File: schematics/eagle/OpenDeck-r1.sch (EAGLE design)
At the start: 249 parts, among them U1 ATMEGA32U4-AU, U2 4067D, U3 4067D, U4 74AC11238D, U5 ULN2803, U6 74AC165D, U7 74AC11238D, U8 6N138, Y1 16MHz

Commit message: LDO for analog, charge pump for LEDs, misc
* added LDO for AREF and to power analog circuitry
* added charge pump to provide stable 5V for LEDs
* remove one row in LED matrix so that 48 LEDs = 16 RGB LEDs
* move SR_LATCH to PD0
* better capacitor markings
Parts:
- removed L49, L50, L51, L52, L53, L54, L55, L56: LAW51M, led:LAW51M
- removed LM4132CMF-4.1: LM4132BMF-4.1, NSC_By_element14_Batch_1.1:LM4132BMF-4.1
- removed R7: 75, rcl:R-EU_0204/7
- added C18: 1u, rcl:C-EU025-025X050
- added C19: 0.47u, rcl:C-EU025-025X050
- added C20, C21, C22: 0.1u, rcl:C-EU025-025X050
- added MAX1595-5V: MAX662CPA, maxim:MAX662CPA
- added MCP1825-3.3V: MCP1825_SOT223, bt_regulator:MCP1825_SOT223
- added Q1, Q2, Q3, Q4, Q5, Q6: FDN360P, transistor-power:FDN360P
- C1, C10, C11, C12, C13, C14, C17, C6, C7, C8, C9: value 0.01 -> 0.01u
- C2: value 0.01 -> 4.7u
- C3: value 0.01 -> 1u
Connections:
- removed net LR_7: R7.2, U1.PD0(INT0/OC0B/SCL)
- removed net L_ROW_6: L49G$1.A, L50G$1.A, L51G$1.A, L52G$1.A, L53G$1.A, L54G$1.A, L55G$1.A, L56G$1.A, R7.1
- removed net SR_CLOCK/MISO: HEADER_1.4, U1.PB3(PDO/MISO), U6A.CLK
- new net +5V_LEDS: C19.1, MAX1595-5V.AOUT, MAX1595-5V.VOUT, Q1.S, Q2.S, Q3.S, Q4.S, Q5.S, Q6.S
- new net MISO: HEADER_1.4, U1.PB3(PDO/MISO)
- new net N$74: C20.1, MAX1595-5V.CXP
- new net N$78: C20.2, MAX1595-5V.CXN
- new net N$79: Q1.D, R1.2
- new net N$80: Q2.D, R2.2
- new net N$81: Q3.D, R3.2
- new net N$82: Q4.D, R4.2
- new net N$83: Q5.D, R5.2
- new net N$86: Q6.D, R6.2
- new net SR_CLOCK: U1.PD1(INT1/SDA), U6A.CLK
- net +5V: now also C18.1, MAX1595-5V.SHDN, MAX1595-5V.VCC, MCP1825-3.3V.VIN; no longer LM4132CMF-4.1.EN, LM4132CMF-4.1.VIN, U2P.VDD, U3P.VDD
- net AREF: now also C21.2, C22.2, MCP1825-3.3V.VOUT, U2P.VDD, U3P.VDD; no longer LM4132CMF-4.1.VREF
- net GND: now also C18.2, C19.2, C21.1, C22.1, MAX1595-5V.GND, MAX1595-5V.PGND, MCP1825-3.3V.GND, MCP1825-3.3V.HEATSINK; no longer LM4132CMF-4.1.GND
- net LC_1: no longer L49G$1.C
- net LC_2: no longer L50G$1.C
- net LC_3: no longer L51G$1.C
- net LC_4: no longer L52G$1.C
- net LC_5: no longer L53G$1.C
- net LC_6: no longer L54G$1.C
- net LC_7: no longer L55G$1.C
- net LC_8: no longer L56G$1.C
- net LR_1: now also Q1.G; no longer R1.2
- net LR_2: now also Q2.G; no longer R2.2
- net LR_3: now also Q3.G; no longer R3.2
- net LR_4: now also Q4.G; no longer R4.2
- net LR_5: now also Q5.G; no longer R5.2
- net LR_6: now also Q6.G; no longer R6.2
- net SR_LATCH: now also U1.PD0(INT0/OC0B/SCL); no longer U1.PD1(INT1/SDA)
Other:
- note added: "LEDs"
- note added: "Note: All diodes 1N4148 Transistors: FDC6312P"
- note removed: "Note: All diodes 1N4148"
- moved on the sheet: C11, C2, C3, C7, C9, L01, L02, L03, L04, L05, L06, L07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

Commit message: * added protection diodes for VBUS, D- and D+ * board can be powered with USB connector only to reduce complexity - either via PC or mobile charger/similar
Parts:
- removed 22: 22, rcl:R-EU_0204/7
- removed C15, C16: 10u, rcl:CPOL-EUSMCB
- removed C6: 0.01u, rcl:C-EU025-025X050
- removed JP2: POWER_JACKPTH, SparkFun-Connectors:POWER_JACKPTH
- removed NCP1117ST50T3G: MC33269ST-3.3T3, linear:MC33269ST-3.3T3
- added C23: 10u, rcl:CPOL-EUSMCB
- added C24: 1u, rcl:C-EU025-025X050
- added PRTR5V0U2X: PRTR5V0U2X, PRTR5V0U2X:PRTR5V0U2X
- added R7: 22, rcl:R-EU_0204/7
- C10, C11, C12, C13, C14, C17, C7, C8, C9: value 0.01u -> 0.1u
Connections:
- removed net N$6: JP1.D+, R22.1
- removed net N$73: 22.1, JP1.D-
- removed net VIN: C16.+, JP2.PWR, NCP1117ST50T3G.IN
- new net D+X: JP1.D+, PRTR5V0U2X.I/O2, R22.1
- new net D-X: JP1.D-, PRTR5V0U2X.I/O1, R7.1
- net +5V: now also C23.+, C24.1, PRTR5V0U2X.VCC; no longer C15.+, C6.1, NCP1117ST50T3G.OUT, NCP1117ST50T3G.OUT@1
- net D-: now also R7.2; no longer 22.2
- net GND: now also C23.-, C24.2, PRTR5V0U2X.GND; no longer C15.-, C16.-, C6.2, JP2.GND, JP2.GNDBREAK, NCP1117ST50T3G.GND/ADJ
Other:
- note added: "Notes: All diodes 1N4148 Transistors: FDC6312P TVS diodes: PRTR5V0U2X"
- note removed: "Note: All diodes 1N4148 Transistors: FDC6312P"
- note removed: "POWER JACK"
- note removed: "VBUS"
- moved on the sheet: JP1, POWER_LED, R22, R23

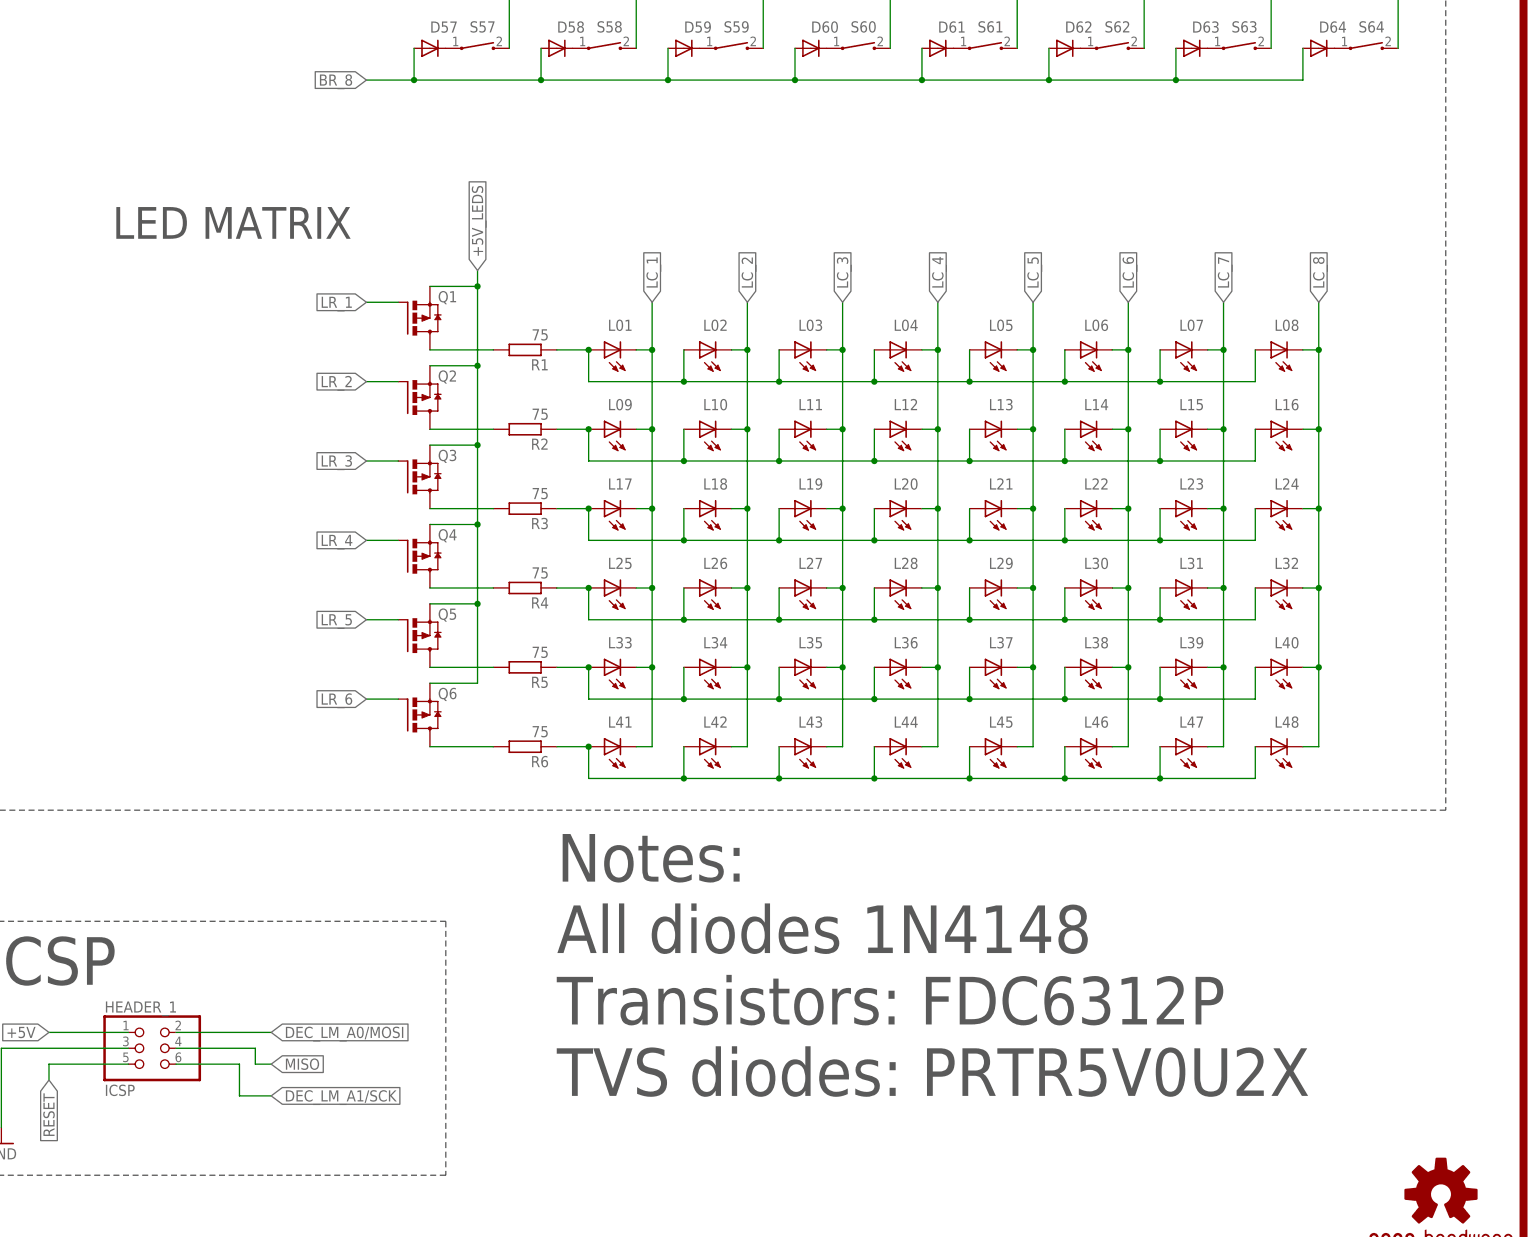
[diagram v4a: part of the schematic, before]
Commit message: changes to led matrix
* replace 75R with 100R resistors for LED rows
* add 4k7 pull-up on each row transistor
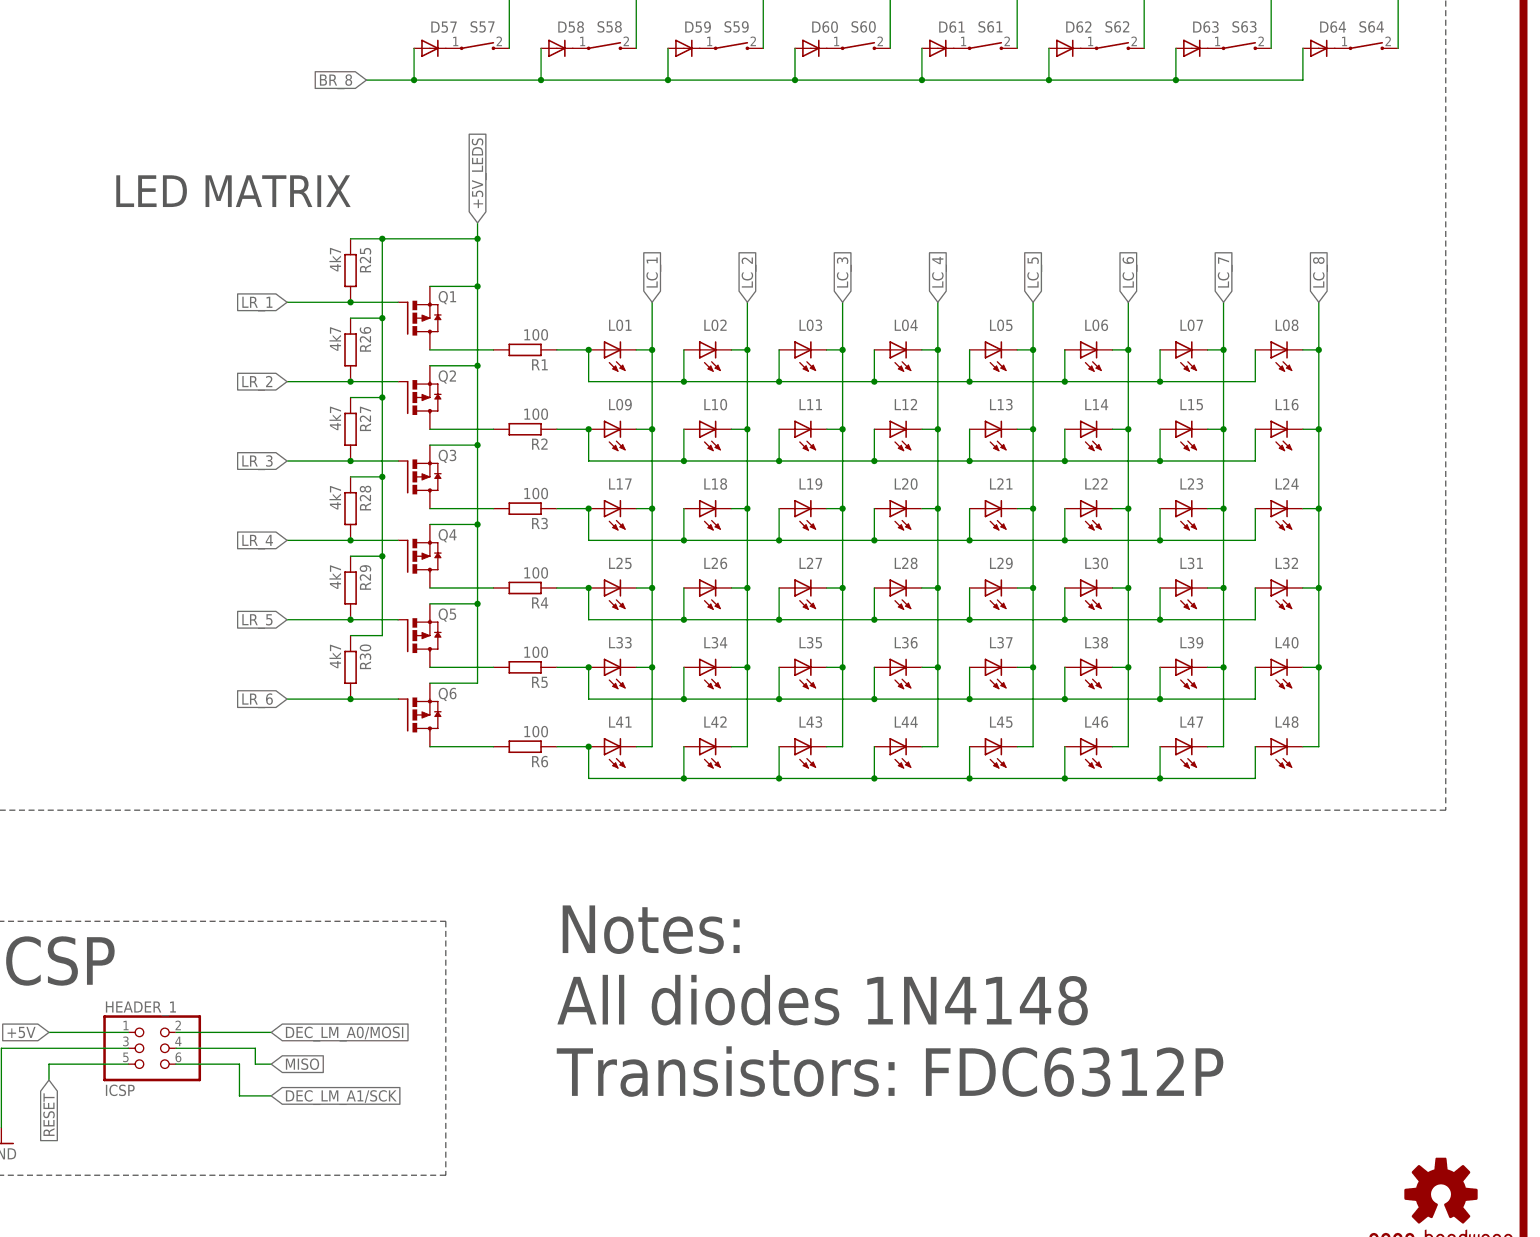
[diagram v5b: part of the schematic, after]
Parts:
- added R25, R26, R27, R28, R29, R30: 4k7, rcl:R-EU_0204/7
- R1, R2, R3, R4, R5, R6: value 75 -> 100
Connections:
- net +5V_LEDS: now also R25.1, R26.1, R27.1, R28.1, R29.1, R30.1
- net LR_1: now also R25.2
- net LR_2: now also R26.2
- net LR_3: now also R27.2
- net LR_4: now also R28.2
- net LR_5: now also R29.2
- net LR_6: now also R30.2
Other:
- note added: "Notes: All diodes 1N4148 Transistors: FDC6312P"
- note removed: "Notes: All diodes 1N4148 Transistors: FDC6312P TVS diodes: PRTR5V0U2X"

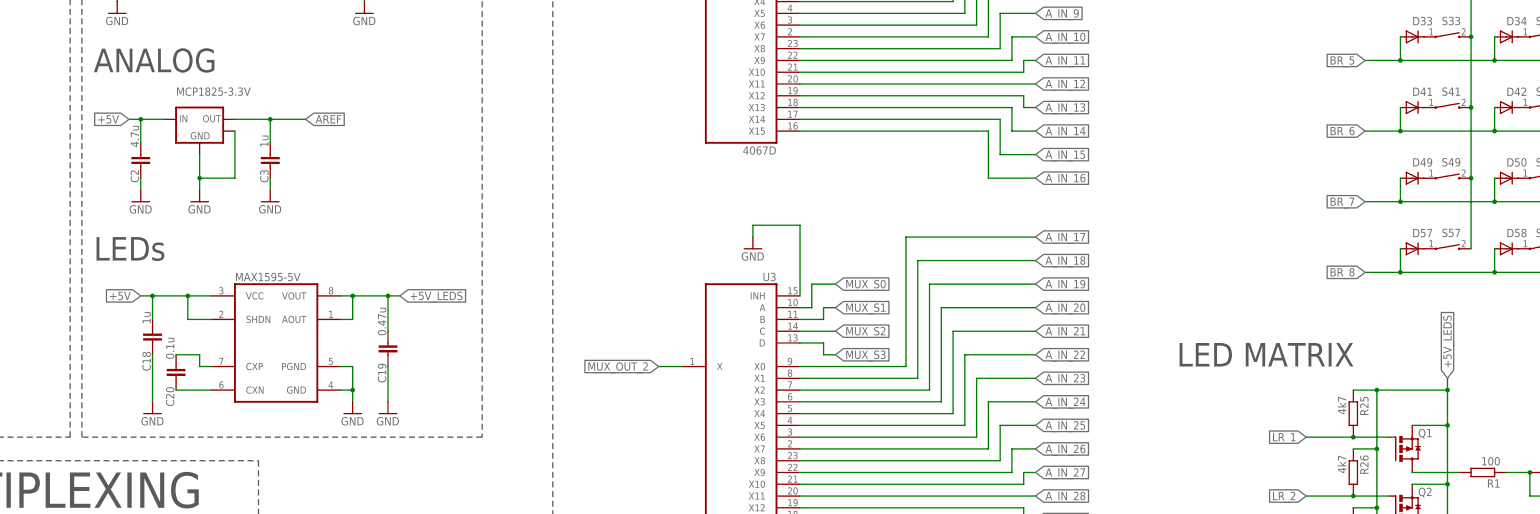
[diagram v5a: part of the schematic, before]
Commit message: replace charge pump for LEDs with LDO (cost)
* max1595 5V charge pump is replaced with LP2985 4V LDO for cost reasons
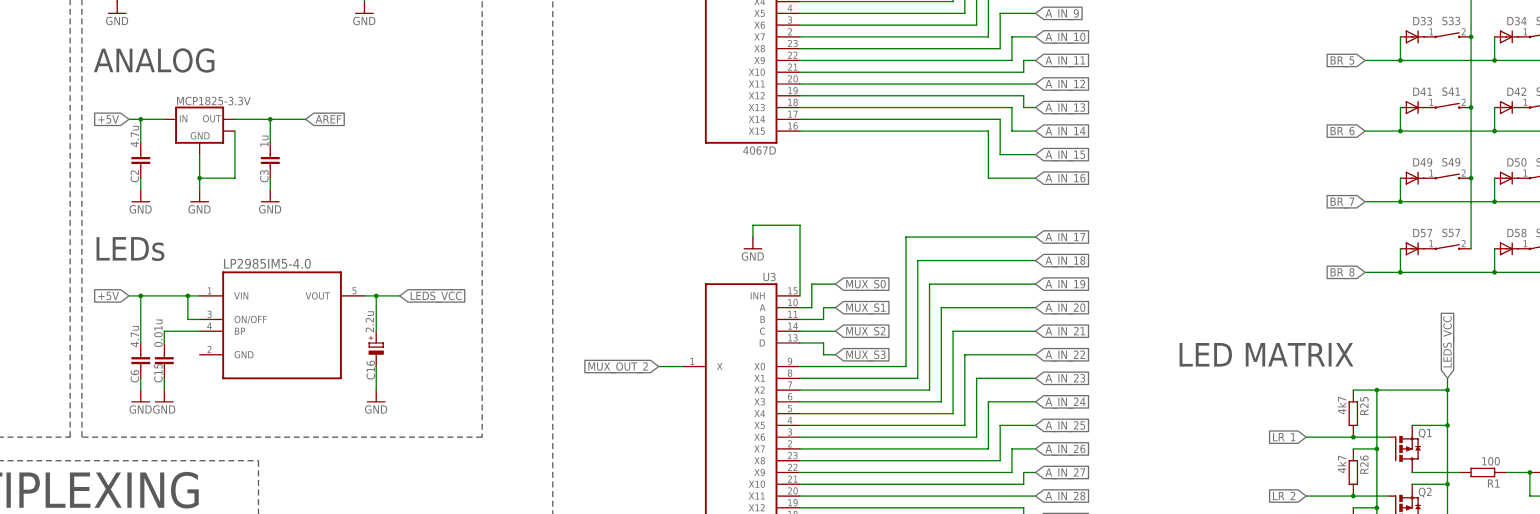
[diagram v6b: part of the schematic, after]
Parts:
- removed C18: 1u, rcl:C-EU025-025X050
- removed C19: 0.47u, rcl:C-EU025-025X050
- removed C20: 0.1u, rcl:C-EU025-025X050
- removed MAX1595-5V: MAX662CPA, maxim:MAX662CPA
- added C15: 0.01u, rcl:C-EU025-025X050
- added C16: 2.2u, rcl:CPOL-EUSMCB
- added C6: 4.7u, rcl:C-EU025-025X050
- added U9: LP2985IM5-4.0, NSC_By_element14_Batch_1.1:LP2985IM5-4.0
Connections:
- removed net +5V_LEDS: C19.1, MAX1595-5V.AOUT, MAX1595-5V.VOUT, Q1.S, Q2.S, Q3.S, Q4.S, Q5.S, Q6.S, R25.1, R26.1, R27.1, R28.1, R29.1, R30.1
- removed net N$74: C20.1, MAX1595-5V.CXP
- removed net N$78: C20.2, MAX1595-5V.CXN
- new net LEDS_VCC: C16.+, Q1.S, Q2.S, Q3.S, Q4.S, Q5.S, Q6.S, R25.1, R26.1, R27.1, R28.1, R29.1, R30.1, U9.VOUT
- new net N$6: C15.1, U9.BP
- net +5V: now also C6.1, U9.ON/OFF, U9.VIN; no longer C18.1, MAX1595-5V.SHDN, MAX1595-5V.VCC
- net GND: now also C15.2, C16.-, C6.2; no longer C18.2, C19.2, MAX1595-5V.GND, MAX1595-5V.PGND

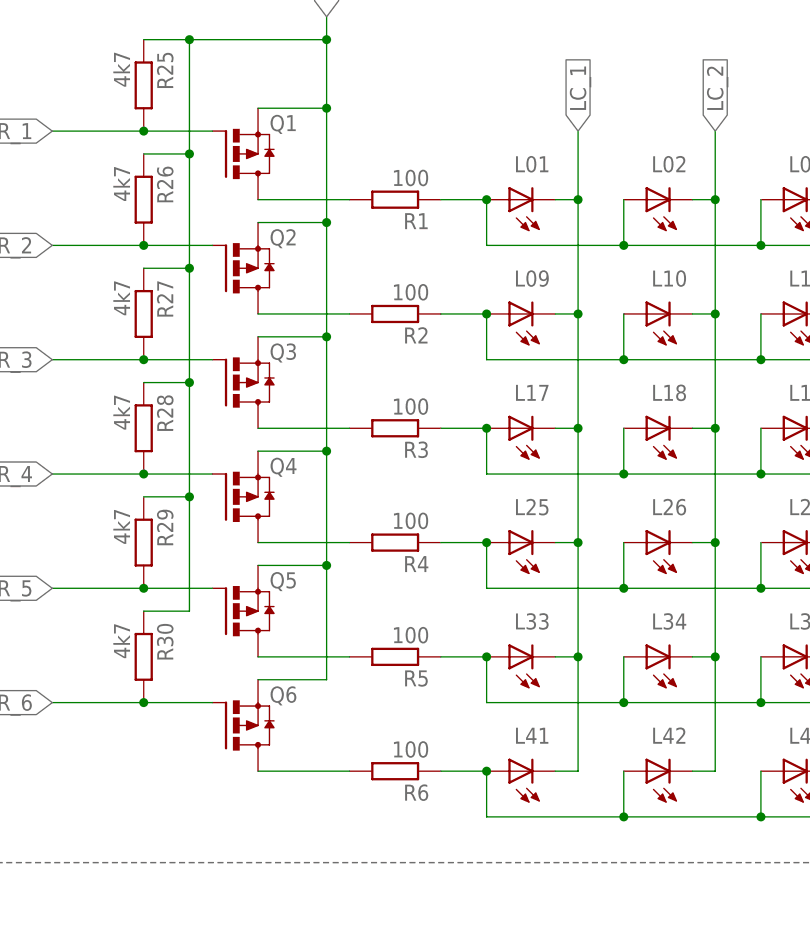
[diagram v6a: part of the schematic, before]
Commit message: replace 100R with 75R for LEDs
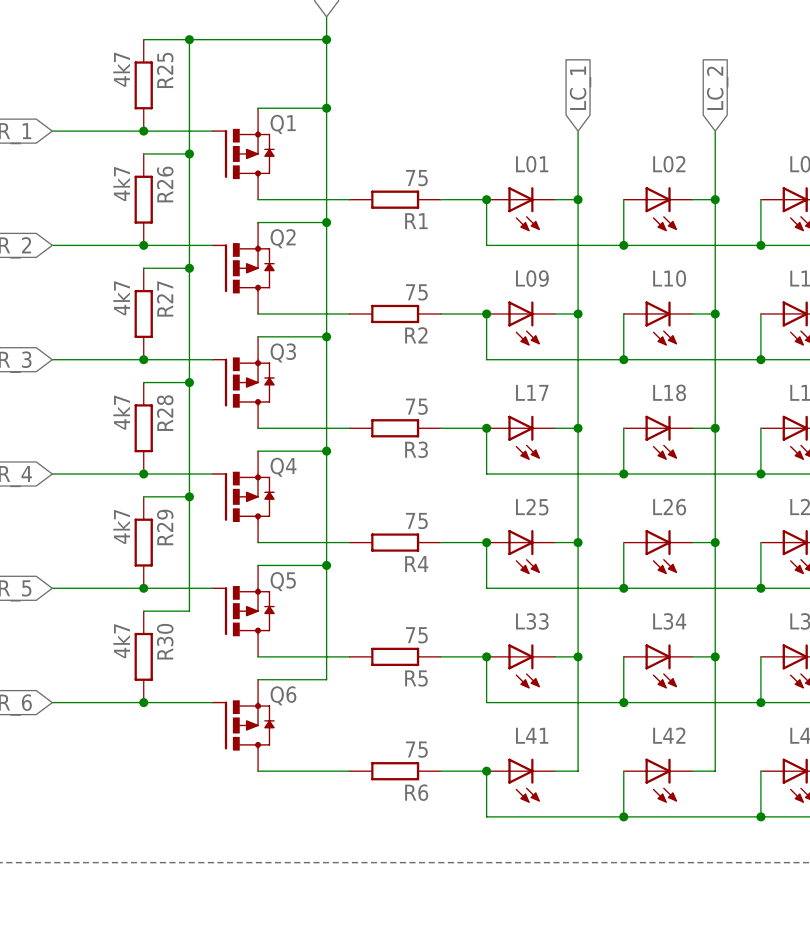
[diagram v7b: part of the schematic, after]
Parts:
- R1, R2, R3, R4, R5, R6: value 100 -> 75
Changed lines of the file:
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@@
 <part name="L22" library="led" deviceset="*W51M" device="" technology="LA"/>
 <part name="L15" library="led" deviceset="*W51M" device="" technology="LA"/>
-<part name="R1" library="rcl" deviceset="R-EU_" device="0204/7" value="100"/>
-<part name="R2" library="rcl" deviceset="R-EU_" device="0204/7" value="100"/>
-<part name="R3" library="rcl" deviceset="R-EU_" device="0204/7" value="100"/>
+<part name="R1" library="rcl" deviceset="R-EU_" device="0204/7" value="75"/>
+<part name="R2" library="rcl" deviceset="R-EU_" device="0204/7" value="75"/>
+<part name="R3" library="rcl" deviceset="R-EU_" device="0204/7" value="75"/>
 <part name="L25" library="led" deviceset="*W51M" device="" technology="LA"/>
 <part name="L26" library="led" deviceset="*W51M" device="" technology="LA"/>
@@
 <part name="L31" library="led" deviceset="*W51M" device="" technology="LA"/>
 <part name="L32" library="led" deviceset="*W51M" device="" technology="LA"/>
-<part name="R4" library="rcl" deviceset="R-EU_" device="0204/7" value="100"/>
+<part name="R4" library="rcl" deviceset="R-EU_" device="0204/7" value="75"/>
 <part name="L33" library="led" deviceset="*W51M" device="" technology="LA"/>
 <part name="L34" library="led" deviceset="*W51M" device="" technology="LA"/>
@@
 <part name="L39" library="led" deviceset="*W51M" device="" technology="LA"/>
 <part name="L40" library="led" deviceset="*W51M" device="" technology="LA"/>
-<part name="R5" library="rcl" deviceset="R-EU_" device="0204/7" value="100"/>
+<part name="R5" library="rcl" deviceset="R-EU_" device="0204/7" value="75"/>
 <part name="L41" library="led" deviceset="*W51M" device="" technology="LA"/>
 <part name="L42" library="led" deviceset="*W51M" device="" technology="LA"/>
@@
 <part name="L47" library="led" deviceset="*W51M" device="" technology="LA"/>
 <part name="L48" library="led" deviceset="*W51M" device="" technology="LA"/>
-<part name="R6" library="rcl" deviceset="R-EU_" device="0204/7" value="100"/>
+<part name="R6" library="rcl" deviceset="R-EU_" device="0204/7" value="75"/>
 <part name="U6" library="74xx-eu" deviceset="74*165" device="D" technology="AC"/>
 <part name="GND2" library="supply1" deviceset="GND" device=""/>
